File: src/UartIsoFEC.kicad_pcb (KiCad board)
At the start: 2 copper layers, 24 x 27.9 mm, 33 parts, among them J1 B3B-XH-A, P1 105444-0001, Q1 DMP3099L-13, U1 FT230XS, U2 ADUM5211

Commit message: Updated footprints
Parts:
- J1: footprint Medo64:J JST XH Sideway [UART] (3w) -> Medo64:J JST XH Edge [UART] (3w)
- moved C3 2.10 mm to (38.3, 25.7)
- moved L1 2.10 mm to (40.4, 25.7)
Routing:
- net A_5V: track 80.5 -> 76.7 mm
- net A_GND: track 97.8 -> 96.5 mm
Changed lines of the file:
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@@
   )
   (footprint "Medo64:L (0805)" (layer "F.Cu")
-    (at 38.3 25.7 90)
+    (at 40.4 25.7 90)
     (descr "RESC2013X70N")
     (attr smd)
@@
   )
   (footprint "Medo64:C (0805)" (layer "F.Cu")
-    (at 40.4 25.7 90)
+    (at 38.3 25.7 90)
     (tags "CAPC2013X140N")
     (attr smd)
@@
     )
   )
-  (footprint "Medo64:J JST XH Sideway [UART] (3w)" (layer "F.Cu")
+  (footprint "Medo64:J JST XH Edge [UART] (3w)" (layer "F.Cu")
     (at 32 40.8)
     (descr "JST B3B-XH-A [455-B3B-XH-A-ND]")
@@
         (effects (font (size 0.8 0.6) (thickness 0.15) bold))
     )
+    (fp_text user "GND" (at 0 -1.65) (layer "Cmts.User" knockout)
+        (effects (font (size 0.13 0.07) (thickness 0.01) bold))
+    )
     (fp_text user "RX" (at -2.5 -1.65) (layer "Cmts.User" knockout)
-        (effects (font (size 0.13 0.07) (thickness 0.01) bold))
-    )
-    (fp_text user "GND" (at 0 -1.65) (layer "Cmts.User" knockout)
         (effects (font (size 0.13 0.07) (thickness 0.01) bold))
     )
@@
     (fp_rect (start -2.45 -0.85) (end 2.45 0.85)
       (stroke (width 0.2) (type default)) (fill none) (layer "F.SilkS"))
-    (fp_rect (start -0.9 -0.7) (end -0.7 0.7)
+    (fp_rect (start -0.9 -0.35) (end -0.7 0.35)
       (stroke (width 0) (type solid)) (fill solid) (layer "F.Mask"))
-    (fp_rect (start 0.9 -0.7) (end 0.7 0.7)
+    (fp_rect (start 0.9 -0.35) (end 0.7 0.35)
       (stroke (width 0) (type solid)) (fill solid) (layer "F.Mask"))
     (fp_rect (start -2.55 -0.95) (end 2.55 0.95)
       (stroke (width 0.01) (type dash)) (fill none) (layer "F.CrtYd"))
-    (pad "1" smd roundrect (at -1.6 0 90) (size 1.4 1.4) (layers "F.Cu" "F.Mask") (roundrect_rratio 0)
-      (chamfer_ratio 0.2) (chamfer top_left bottom_left)
+    (pad "1" smd roundrect (at -1.6 0 90) (size 1.4 1.4) (layers "F.Cu" "F.Mask") (roundrect_rratio 0.2)
+      (chamfer_ratio 0.25) (chamfer top_right bottom_right)
       (net 11 "VSEL_5V") (thermal_bridge_angle 45))
     (pad "2" smd roundrect (at 0 0 90) (size 1.4 1.4) (layers "F.Cu" "F.Mask") (roundrect_rratio 0)
-      (chamfer_ratio 0.2) (chamfer)
+      (chamfer_ratio 0.25) (chamfer top_left top_right bottom_left bottom_right)
       (net 7 "B_VSEL") (thermal_bridge_angle 45))
-    (pad "3" smd roundrect (at 1.6 0 90) (size 1.4 1.4) (layers "F.Cu" "F.Mask") (roundrect_rratio 0)
-      (chamfer_ratio 0.2) (chamfer top_right bottom_right)
+    (pad "3" smd roundrect (at 1.6 0 90) (size 1.4 1.4) (layers "F.Cu" "F.Mask") (roundrect_rratio 0.2)
+      (chamfer_ratio 0.25) (chamfer top_left bottom_left)
       (net 12 "VSEL_3V3") (thermal_bridge_angle 45))
   )
@@
   (segment (start 32.943674 38.5) (end 32.325 37.881326) (width 0.2) (layer "B.Cu") (net 3))
   (segment (start 32.325 37.881326) (end 32.325 37.737652) (width 0.2) (layer "B.Cu") (net 3))
-  (segment (start 35.175 26) (end 35 26.175) (width 0.2) (layer "F.Cu") (net 4))
-  (segment (start 37 25.775) (end 36.525 25.775) (width 0.2) (layer "F.Cu") (net 4))
   (segment (start 34.2 27.7) (end 34.15 27.7) (width 0.2) (layer "F.Cu") (net 4))
   (segment (start 34.75 22.1) (end 34.75 23.05) (width 0.2) (layer "F.Cu") (net 4))
   (segment (start 27.1 31) (end 27.1 26.9) (width 0.2) (layer "F.Cu") (net 4))
+  (segment (start 37 29.05) (end 37 26.6) (width 0.2) (layer "F.Cu") (net 4))
+  (segment (start 38.3 26.6) (end 37 26.6) (width 0.2) (layer "F.Cu") (net 4))
+  (segment (start 38.3 26.6) (end 39.125 25.775) (width 0.2) (layer "F.Cu") (net 4))
   (segment (start 29.725 26.175) (end 29 26.9) (width 0.2) (layer "F.Cu") (net 4))
-  (segment (start 40.4 25.775) (end 37 25.775) (width 0.2) (layer "F.Cu") (net 4))
+  (segment (start 36.575 26.175) (end 35 26.175) (width 0.2) (layer "F.Cu") (net 4))
   (segment (start 34.9 23.5) (end 41.2 23.5) (width 0.2) (layer "F.Cu") (net 4))
   (segment (start 27.1 26.9) (end 29 26.9) (width 0.2) (layer "F.Cu") (net 4))
   (segment (start 35.63236 30.6825) (end 36.95 29.36486) (width 0.2) (layer "F.Cu") (net 4))
   (segment (start 34.75 22.95697) (end 34.75 22.1) (width 0.2) (layer "F.Cu") (net 4))
-  (segment (start 37 29.05) (end 37 25.775) (width 0.2) (layer "F.Cu") (net 4))
-  (segment (start 40.4 26.6) (end 40.4 25.775) (width 0.2) (layer "F.Cu") (net 4))
   (segment (start 34.7 30.6825) (end 35.63236 30.6825) (width 0.2) (layer "F.Cu") (net 4))
   (segment (start 41.2 23.5) (end 42.5 24.8) (width 0.2) (layer "F.Cu") (net 4))
+  (segment (start 37 26.6) (end 36.575 26.175) (width 0.2) (layer "F.Cu") (net 4))
   (segment (start 23.95 26.9) (end 21.25 24.2) (width 0.2) (layer "F.Cu") (net 4))
   (segment (start 29.25 23.05) (end 29.4 23.2) (width 0.2) (layer "F.Cu") (net 4))
@@
   (segment (start 27.4175 31.3175) (end 27.1 31) (width 0.2) (layer "F.Cu") (net 4))
   (segment (start 34.75 23.05) (end 34.6 23.2) (width 0.2) (layer "F.Cu") (net 4))
-  (segment (start 40.4 25.775) (end 41.325 25.775) (width 0.2) (layer "F.Cu") (net 4))
   (segment (start 27.1 26.9) (end 23.95 26.9) (width 0.2) (layer "F.Cu") (net 4))
   (segment (start 34.6 23.2) (end 34.9 23.5) (width 0.2) (layer "F.Cu") (net 4))
@@
   (segment (start 34.50697 23.2) (end 34.75 22.95697) (width 0.2) (layer "F.Cu") (net 4))
   (segment (start 29.3 31.3175) (end 27.4175 31.3175) (width 0.2) (layer "F.Cu") (net 4))
+  (segment (start 39.125 25.775) (end 41.325 25.775) (width 0.2) (layer "F.Cu") (net 4))
   (segment (start 35 26.175) (end 29.725 26.175) (width 0.2) (layer "F.Cu") (net 4))
   (segment (start 41.325 25.775) (end 42.3 24.8) (width 0.2) (layer "F.Cu") (net 4))
-  (segment (start 36.525 25.775) (end 36.3 26) (width 0.2) (layer "F.Cu") (net 4))
   (segment (start 36.7 34.55) (end 35.2 34.55) (width 0.2) (layer "F.Cu") (net 4))
-  (segment (start 36.3 26) (end 35.175 26) (width 0.2) (layer "F.Cu") (net 4))
   (segment (start 35 26.175) (end 35 26.9) (width 0.2) (layer "F.Cu") (net 4))
   (via (at 34.15 27.7) (size 0.6) (drill 0.3) (layers "F.Cu" "B.Cu") (net 4))
@@
   (segment (start 25.703081 37.303081) (end 25.703081 38.332068) (width 0.2) (layer "B.Cu") (net 8))
   (segment (start 21.572182 30.3) (end 24.327818 30.3) (width 0.2) (layer "F.Cu") (net 9))
-  (segment (start 39.55 27.8) (end 42.5 27.8) (width 0.2) (layer "F.Cu") (net 9))
+  (segment (start 40.45 26.6) (end 42.5 26.6) (width 0.2) (layer "F.Cu") (net 9))
+  (segment (start 40.4 26.55) (end 40.45 26.6) (width 0.2) (layer "F.Cu") (net 9))
   (segment (start 42.5 31.3) (end 42.5 26.6) (width 0.2) (layer "F.Cu") (net 9))
   (segment (start 43.3 32.325) (end 43.3 36.05) (width 0.2) (layer "F.Cu") (net 9))
@@
   (segment (start 38.35 41.35) (end 38.35 36.55) (width 0.2) (layer "F.Cu") (net 9))
   (segment (start 38.4 36.5) (end 38.35 36.55) (width 0.2) (layer "F.Cu") (net 9))
-  (segment (start 38.3 26.55) (end 39.55 27.8) (width 0.2) (layer "F.Cu") (net 9))
-  (segment (start 42.5 27.8) (end 42.5 26.6) (width 0.2) (layer "F.Cu") (net 9))
   (segment (start 42.85 36.5) (end 38.4 36.5) (width 0.2) (layer "F.Cu") (net 9))
   (segment (start 37 30.85) (end 38.35 30.85) (width 0.2) (layer "F.Cu") (net 9))

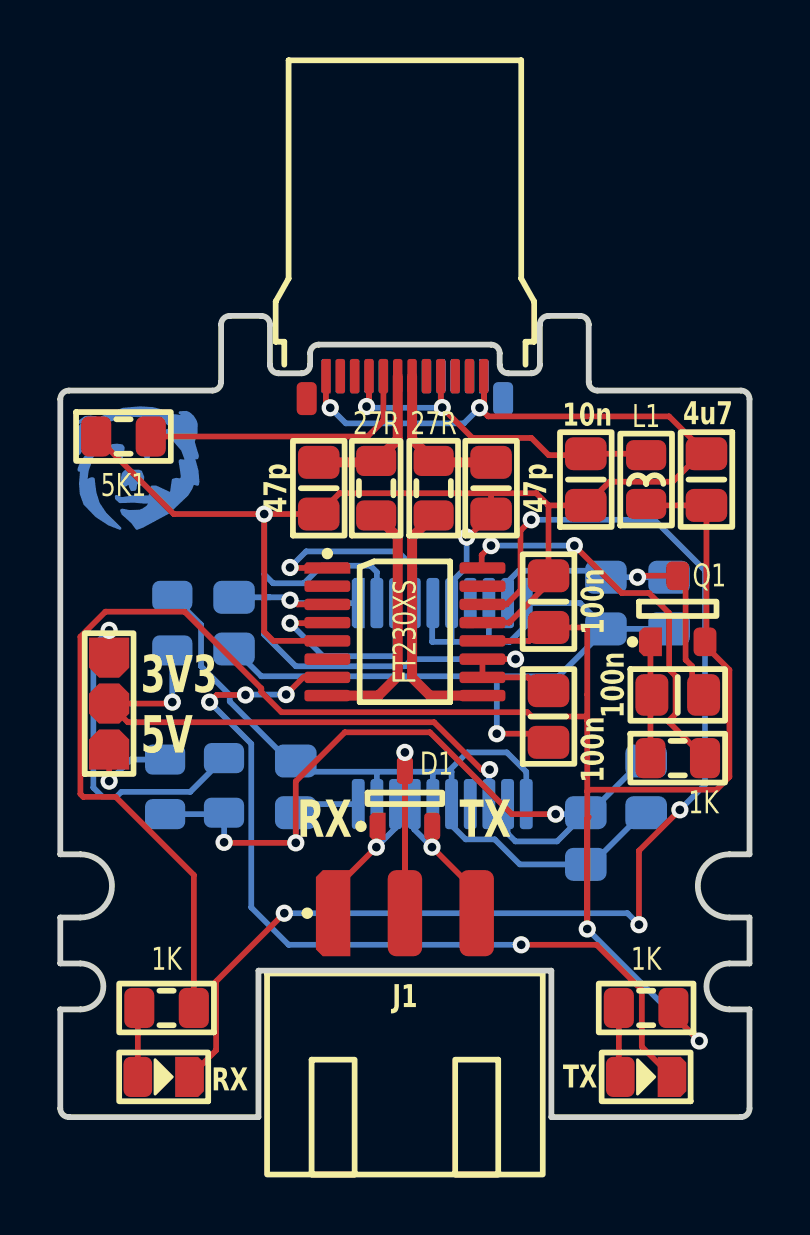
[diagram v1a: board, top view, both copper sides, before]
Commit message: Rotated CC resistor
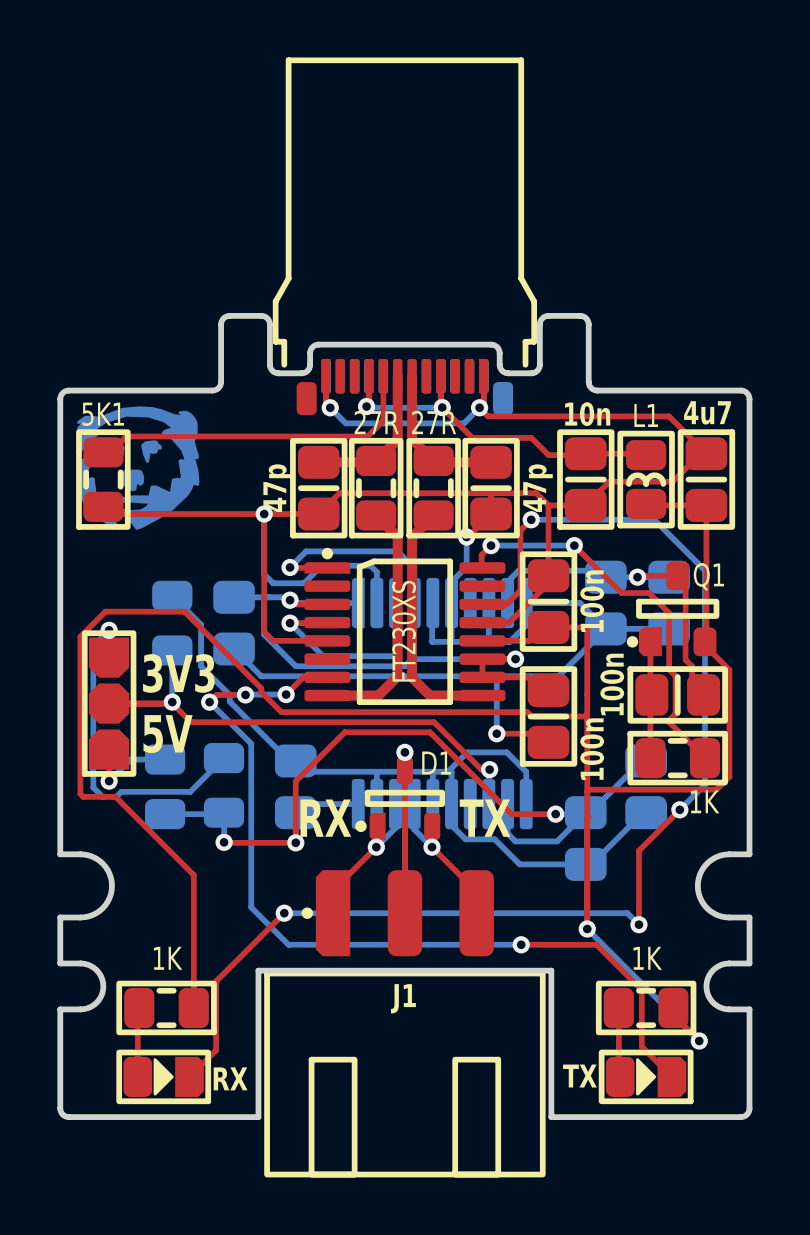
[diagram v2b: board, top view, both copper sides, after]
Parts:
- moved R6 1.66 mm to (21.5, 25.7), turned to 90 degrees
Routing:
- net A_CC: track 9.88 -> 11.5 mm
- net A_GND: track 96.5 -> 94.9 mm
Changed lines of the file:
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@@
   )
   (footprint "Medo64:R (0805)" (layer "F.Cu")
-    (at 22.2 24.2)
+    (at 21.5 25.7 90)
     (tags "RESC2013X70N")
     (attr smd)
-    (fp_text reference "R6" (at 0 -1.6) (layer "F.SilkS") hide
+    (fp_text reference "R6" (at 0 -1.6 90) (layer "F.SilkS") hide
         (effects (font (size 0.8 0.6) (thickness 0.15)))
     )
-    (fp_text value "5K1" (at 0 1.7) (layer "F.SilkS")
+    (fp_text value "5K1" (at 2.25 0 180) (layer "F.SilkS")
         (effects (font (size 0.8 0.6) (thickness 0.15)))
     )
@@
     (fp_rect (start -1 -0.625) (end 1 0.625)
       (stroke (width 0.01) (type dash_dot)) (fill none) (layer "F.Fab"))
-    (pad "1" smd roundrect (at -0.95 0) (size 1.05 1.4) (layers "F.Cu" "F.Paste" "F.Mask") (roundrect_rratio 0.25)
+    (pad "1" smd roundrect (at -0.95 0 90) (size 1.05 1.4) (layers "F.Cu" "F.Paste" "F.Mask") (roundrect_rratio 0.25)
       (net 4 "A_GND") (thermal_bridge_angle 45))
-    (pad "2" smd roundrect (at 0.95 0) (size 1.05 1.4) (layers "F.Cu" "F.Paste" "F.Mask") (roundrect_rratio 0.25)
+    (pad "2" smd roundrect (at 0.95 0 90) (size 1.05 1.4) (layers "F.Cu" "F.Paste" "F.Mask") (roundrect_rratio 0.25)
       (net 16 "A_CC") (thermal_bridge_angle 45))
     (model ":KICAD7_3DMODEL_DIR:Resistor_SMD.3dshapes/R_0805_2012Metric.step"
@@
   (segment (start 41.2 23.5) (end 42.5 24.8) (width 0.2) (layer "F.Cu") (net 4))
   (segment (start 37 26.6) (end 36.575 26.175) (width 0.2) (layer "F.Cu") (net 4))
-  (segment (start 23.95 26.9) (end 21.25 24.2) (width 0.2) (layer "F.Cu") (net 4))
   (segment (start 29.25 23.05) (end 29.4 23.2) (width 0.2) (layer "F.Cu") (net 4))
   (segment (start 35 26.9) (end 34.2 27.7) (width 0.2) (layer "F.Cu") (net 4))
   (segment (start 27.4175 31.3175) (end 27.1 31) (width 0.2) (layer "F.Cu") (net 4))
   (segment (start 34.75 23.05) (end 34.6 23.2) (width 0.2) (layer "F.Cu") (net 4))
-  (segment (start 27.1 26.9) (end 23.95 26.9) (width 0.2) (layer "F.Cu") (net 4))
   (segment (start 34.6 23.2) (end 34.9 23.5) (width 0.2) (layer "F.Cu") (net 4))
   (segment (start 29.25 22.1) (end 29.25 23.05) (width 0.2) (layer "F.Cu") (net 4))
@@
   (segment (start 41.325 25.775) (end 42.3 24.8) (width 0.2) (layer "F.Cu") (net 4))
   (segment (start 36.7 34.55) (end 35.2 34.55) (width 0.2) (layer "F.Cu") (net 4))
+  (segment (start 27.1 26.9) (end 21.75 26.9) (width 0.2) (layer "F.Cu") (net 4))
   (segment (start 35 26.175) (end 35 26.9) (width 0.2) (layer "F.Cu") (net 4))
   (via (at 34.15 27.7) (size 0.6) (drill 0.3) (layers "F.Cu" "B.Cu") (net 4))
@@
   (segment (start 32.25 24.3) (end 33 25.05) (width 0.35) (layer "F.Cu") (net 6))
   (segment (start 35 25.1) (end 33.05 25.1) (width 0.35) (layer "F.Cu") (net 6))
-  (segment (start 21.7 33.5) (end 22.35 34.15) (width 0.2) (layer "F.Cu") (net 7))
-  (segment (start 22.35 34.15) (end 33.017156 34.15) (width 0.2) (layer "F.Cu") (net 7))
+  (segment (start 23.9 33.5) (end 24.55 34.15) (width 0.2) (layer "F.Cu") (net 7))
+  (segment (start 21.7 33.5) (end 23.9 33.5) (width 0.2) (layer "F.Cu") (net 7))
+  (segment (start 33.017156 34.15) (end 34.667156 35.8) (width 0.2) (layer "F.Cu") (net 7))
   (segment (start 23.9 33.45) (end 23.85 33.5) (width 0.2) (layer "F.Cu") (net 7))
-  (segment (start 33.017156 34.15) (end 34.667156 35.8) (width 0.2) (layer "F.Cu") (net 7))
+  (segment (start 24.55 34.15) (end 33.017156 34.15) (width 0.2) (layer "F.Cu") (net 7))
   (segment (start 34.667156 35.8) (end 34.95 35.8) (width 0.2) (layer "F.Cu") (net 7))
   (segment (start 23.85 33.5) (end 21.7 33.5) (width 0.2) (layer "F.Cu") (net 7))
@@
   (segment (start 21.572182 30.3) (end 24.327818 30.3) (width 0.2) (layer "F.Cu") (net 9))
   (segment (start 40.45 26.6) (end 42.5 26.6) (width 0.2) (layer "F.Cu") (net 9))
-  (segment (start 40.4 26.55) (end 40.45 26.6) (width 0.2) (layer "F.Cu") (net 9))
   (segment (start 42.5 31.3) (end 42.5 26.6) (width 0.2) (layer "F.Cu") (net 9))
   (segment (start 43.3 32.325) (end 43.3 36.05) (width 0.2) (layer "F.Cu") (net 9))
@@
   (segment (start 32.25 32.6) (end 32.25 27.7) (width 0.35) (layer "F.Cu") (net 15))
   (segment (start 31.25 23.65) (end 30.7 24.2) (width 0.2) (layer "F.Cu") (net 16))
-  (segment (start 30.7 24.2) (end 23.15 24.2) (width 0.2) (layer "F.Cu") (net 16))
   (segment (start 31.25 22.1) (end 31.25 23.65) (width 0.2) (layer "F.Cu") (net 16))
+  (segment (start 30.7 24.2) (end 22.3 24.2) (width 0.2) (layer "F.Cu") (net 16))
+  (segment (start 22.3 24.2) (end 21.75 24.75) (width 0.2) (layer "F.Cu") (net 16))
   (segment (start 28.01682 28.7775) (end 28 28.76068) (width 0.2) (layer "F.Cu") (net 17))
   (segment (start 29.3 28.7775) (end 28.01682 28.7775) (width 0.2) (layer "F.Cu") (net 17))

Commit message: Updated net names
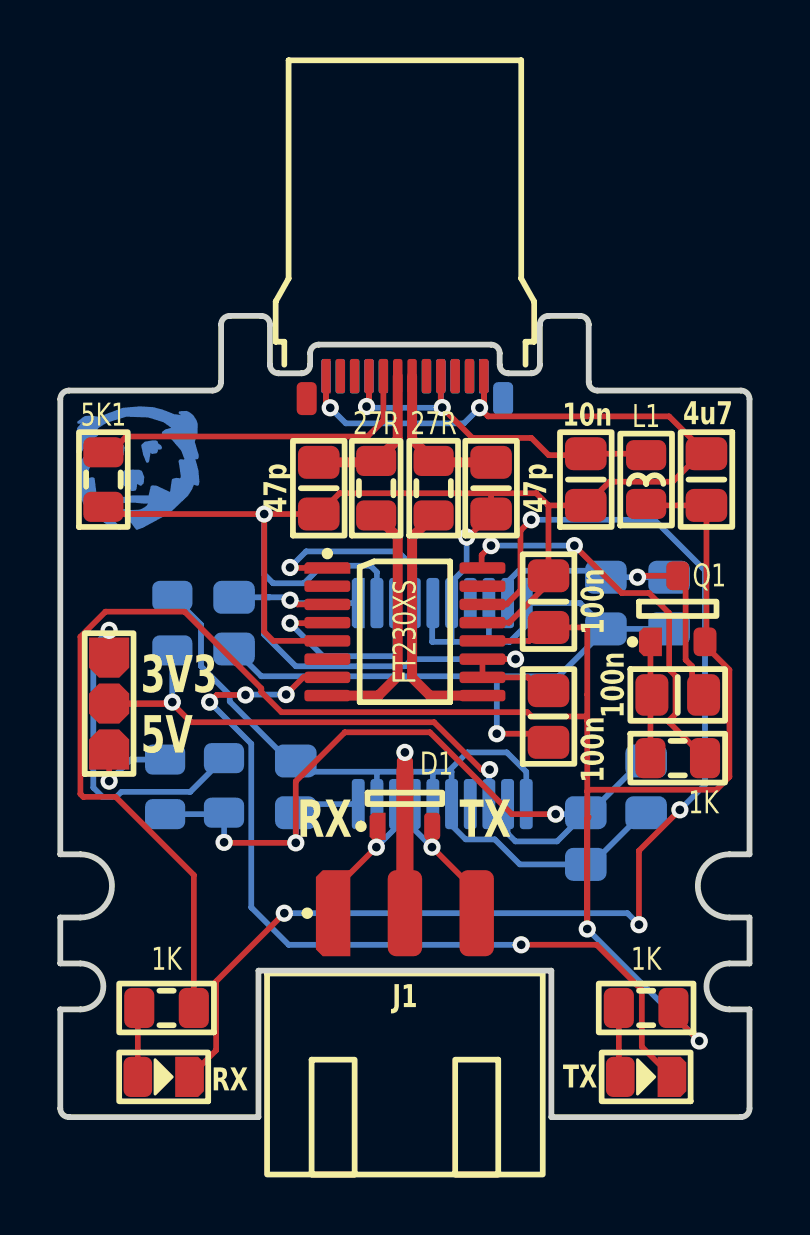
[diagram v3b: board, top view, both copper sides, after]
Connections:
- net A_3V3 renamed 3V3
- net A_5V renamed 5V
- net A_5V_SWITCHED renamed 5V_SWITCHED
- net A_CC renamed USB_CC
- net A_DM renamed USB_DM
- net A_DM' renamed USB_DM'
- net A_DP renamed USB_DP
- net A_DP' renamed USB_DP'
- net A_GND renamed GND
- net A_LED_RX renamed LED_RX
- net A_LED_RX' renamed LED_RX'
- net A_LED_TX renamed LED_TX
- net A_LED_TX' renamed LED_TX'
- net A_RXD renamed RX
- net A_TXD renamed TX
- net A_Vusb renamed USB_V+
- net B_GND renamed ISO_GND
- net B_RX renamed ISO_RX
- net B_TX renamed ISO_TX
- net B_VISO renamed ISO_V+
- net B_VSEL renamed ISO_V_SELECT
- net PWREN_NEG renamed PWREN#
- net PWREN_NEG' renamed PWREN#'
- net VSEL_3V3 renamed ISO_V_SELECT_3V3
- net VSEL_5V renamed ISO_V_SELECT_5V
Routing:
- net ISO_GND: track 39.5 -> 34.3 mm
